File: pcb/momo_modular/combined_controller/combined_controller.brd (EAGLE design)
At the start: 50.8 x 33 mm, 44 parts, among them Q2 P-MOSFET, U1 XRP7659, U2 PIC24FJ64GA306, U3 MCP1702, U5 FLASH8MSOP8, U6 MCP73811

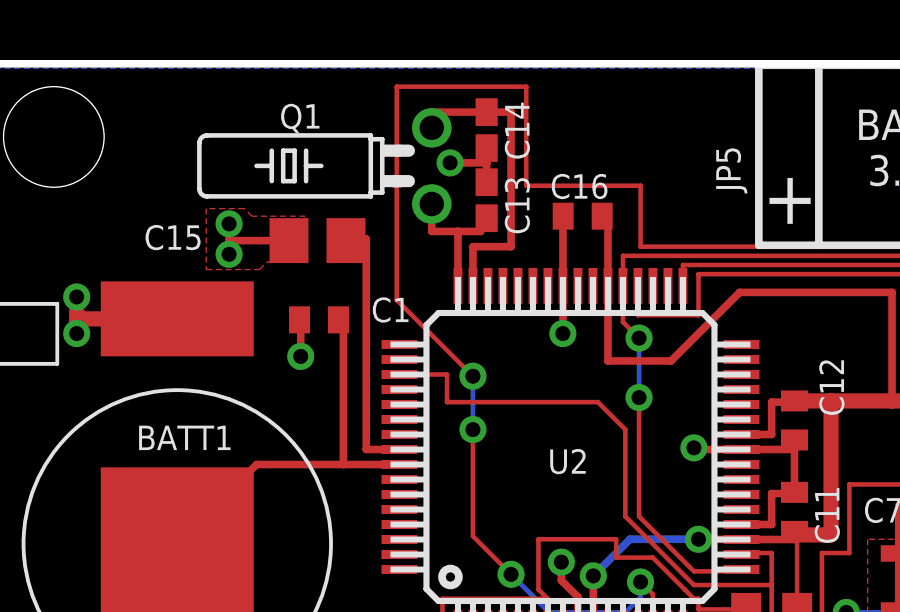
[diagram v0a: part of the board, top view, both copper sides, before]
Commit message: Final review of combined controller
- checked footprint of uc
- added bypass for battery if required
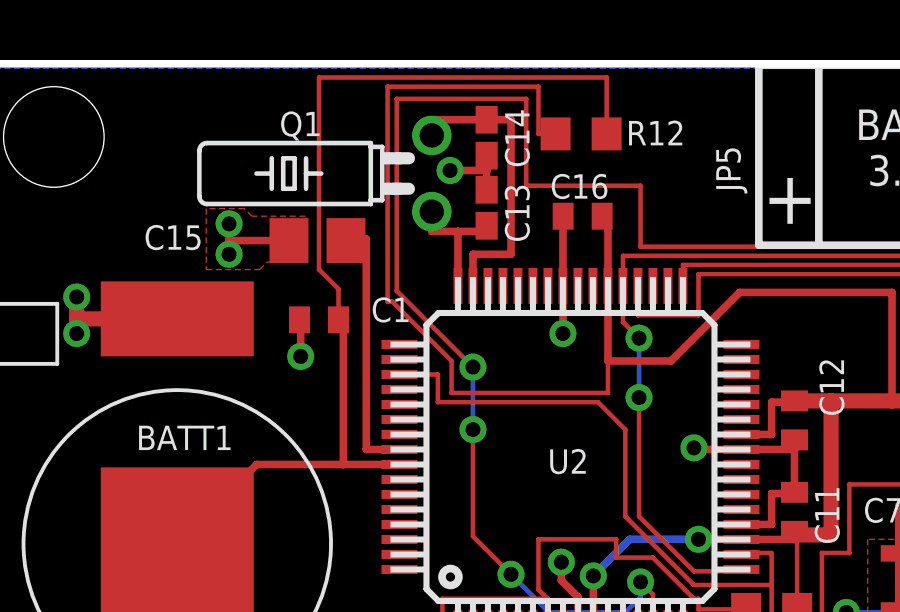
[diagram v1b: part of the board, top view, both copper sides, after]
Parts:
- added R12: 0R, rcl:R0603
- Q1: value (none) -> 32.768khz
- moved C13 0.25 mm to (51.0, 40.2)
- moved C14 0.25 mm to (51.0, 42.5)
- moved Q1 0.25 mm to (49.2, 41.3)
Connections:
- net VBAT: now also R12.2
- net VCCINT: now also R12.1
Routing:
- net VCCINT: track 117.2 -> 141.8 mm
- net VBAT: track 13.5 -> 33.3 mm
- net VBAT_SAMP: track 63.5 -> 62.7 mm
